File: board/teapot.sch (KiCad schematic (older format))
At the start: 13 parts

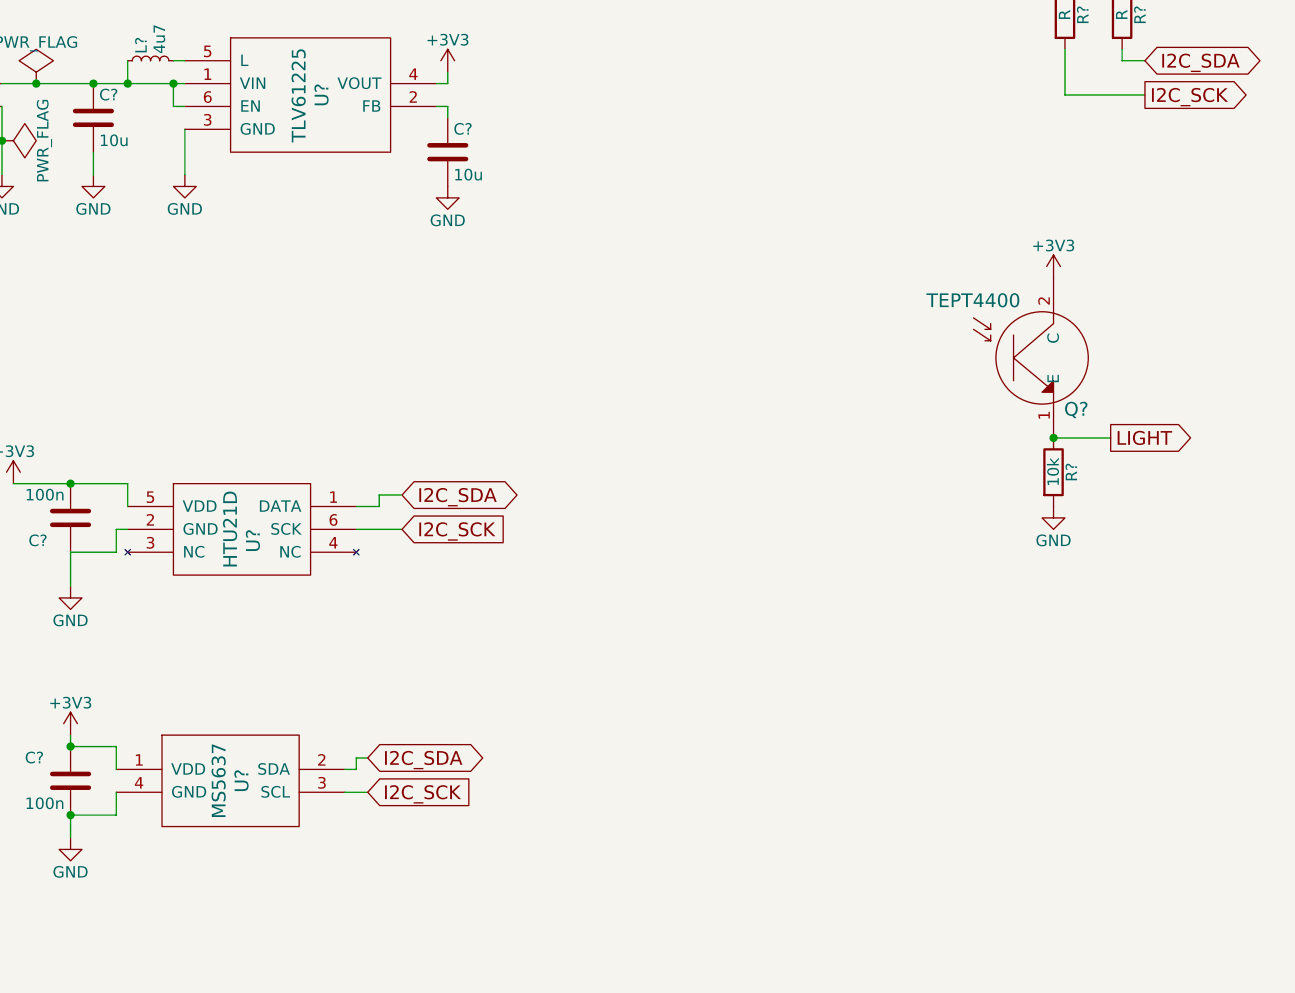
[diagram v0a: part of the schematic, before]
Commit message: schematic part for STM32F070F6P6
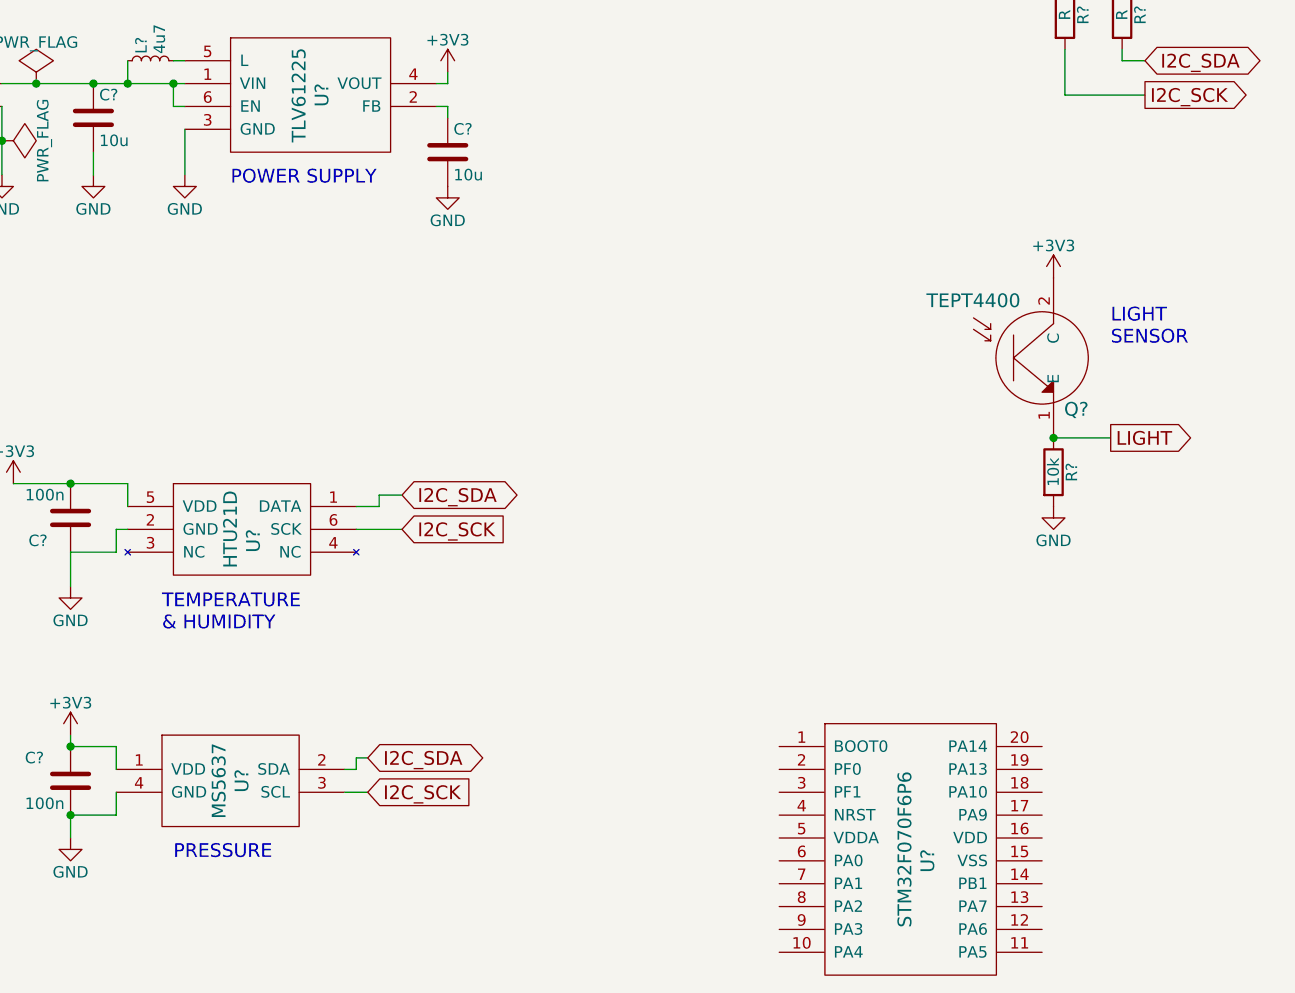
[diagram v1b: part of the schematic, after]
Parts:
- added U?: STM32F070F6P6, symbol STM32F070F6P6
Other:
- note added: "LIGHT\nSENSOR"
- note added: "POWER SUPPLY"
- note added: "PRESSURE"
- note added: "TEMPERATURE\n& HUMIDITY"
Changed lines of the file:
@@
 LIBS:ms5637
 LIBS:tept
+LIBS:stm32f070f6p6
 LIBS:teapot-cache
 EELAYER 25 0
@@
 Text GLabel 5850 2900 2    60   Output ~ 0
 LIGHT
+Text Notes 1750 4750 0    60   ~ 0
+PRESSURE
+Text Notes 1700 3750 0    60   ~ 0
+TEMPERATURE\n& HUMIDITY
+Text Notes 2000 1800 0    60   ~ 0
+POWER SUPPLY
+Text Notes 5850 2500 0    60   ~ 0
+LIGHT\nSENSOR
+$Comp
+L STM32F070F6P6 U?
+U 1 1 5670B075
+P 4950 4750
+F 0 "U?" V 5050 4750 60  0000 C CNN
+F 1 "STM32F070F6P6" V 4950 4800 60  0000 C CNN
+F 2 "" H 5250 5450 60  0000 C CNN
+F 3 "" H 5250 5450 60  0000 C CNN
+	1    4950 4750
+	1    0    0    -1
+$EndComp
 $EndSCHEMATC

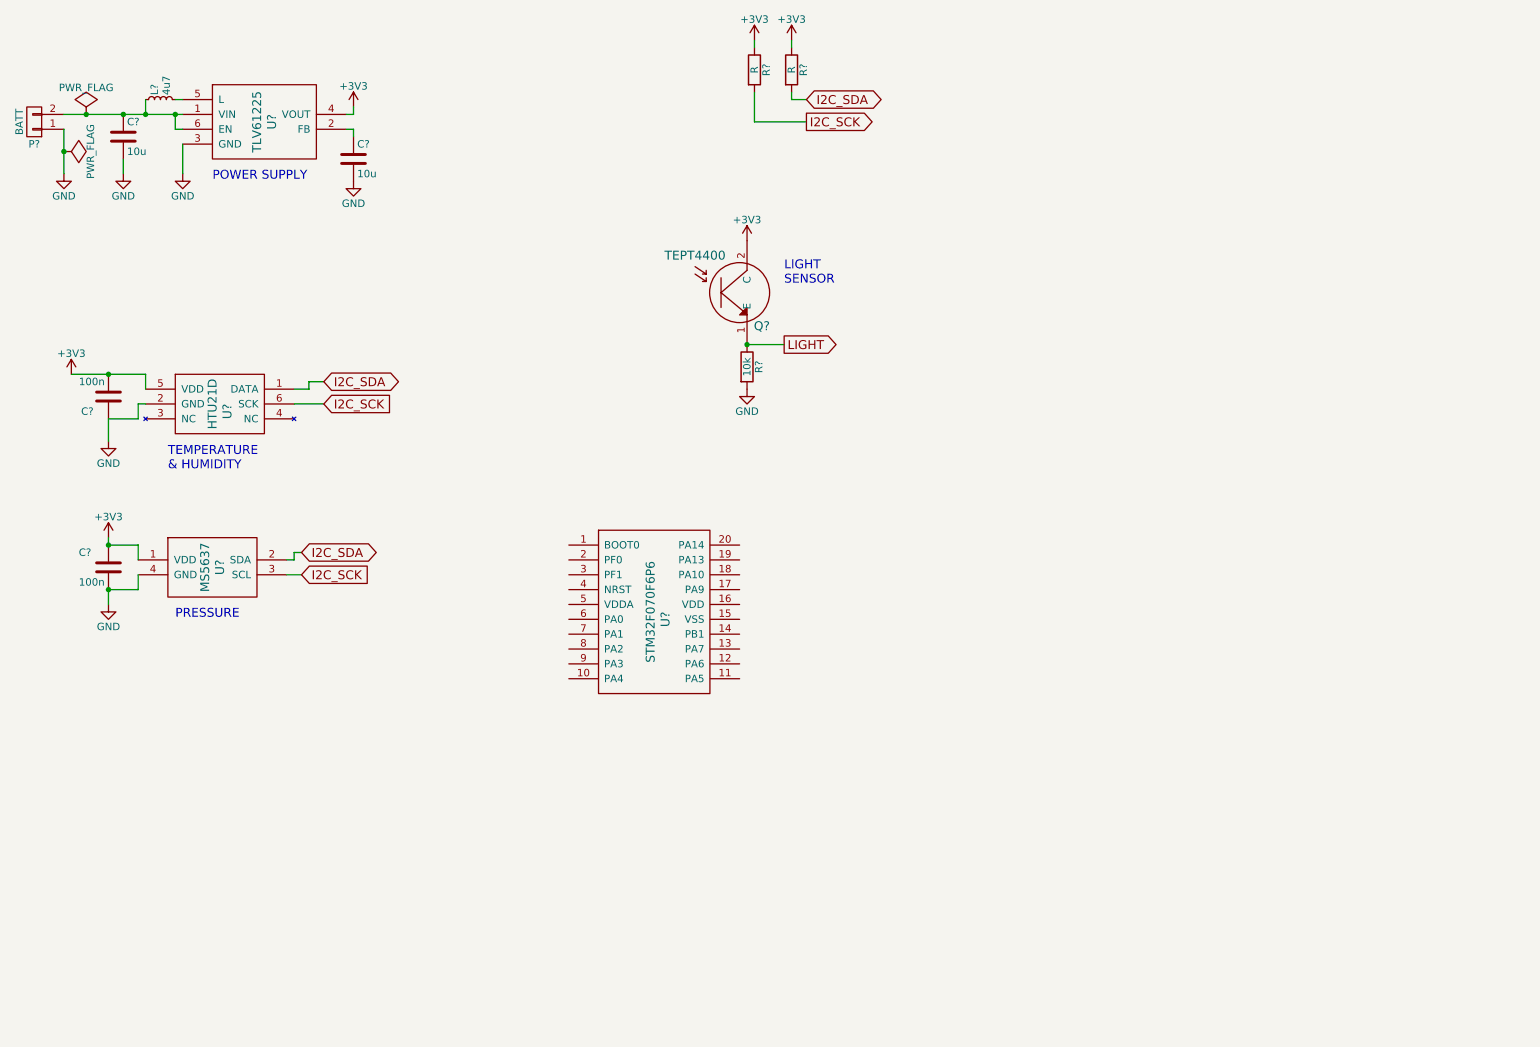
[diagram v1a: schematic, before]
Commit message: Added RFM95W, uC support stuff
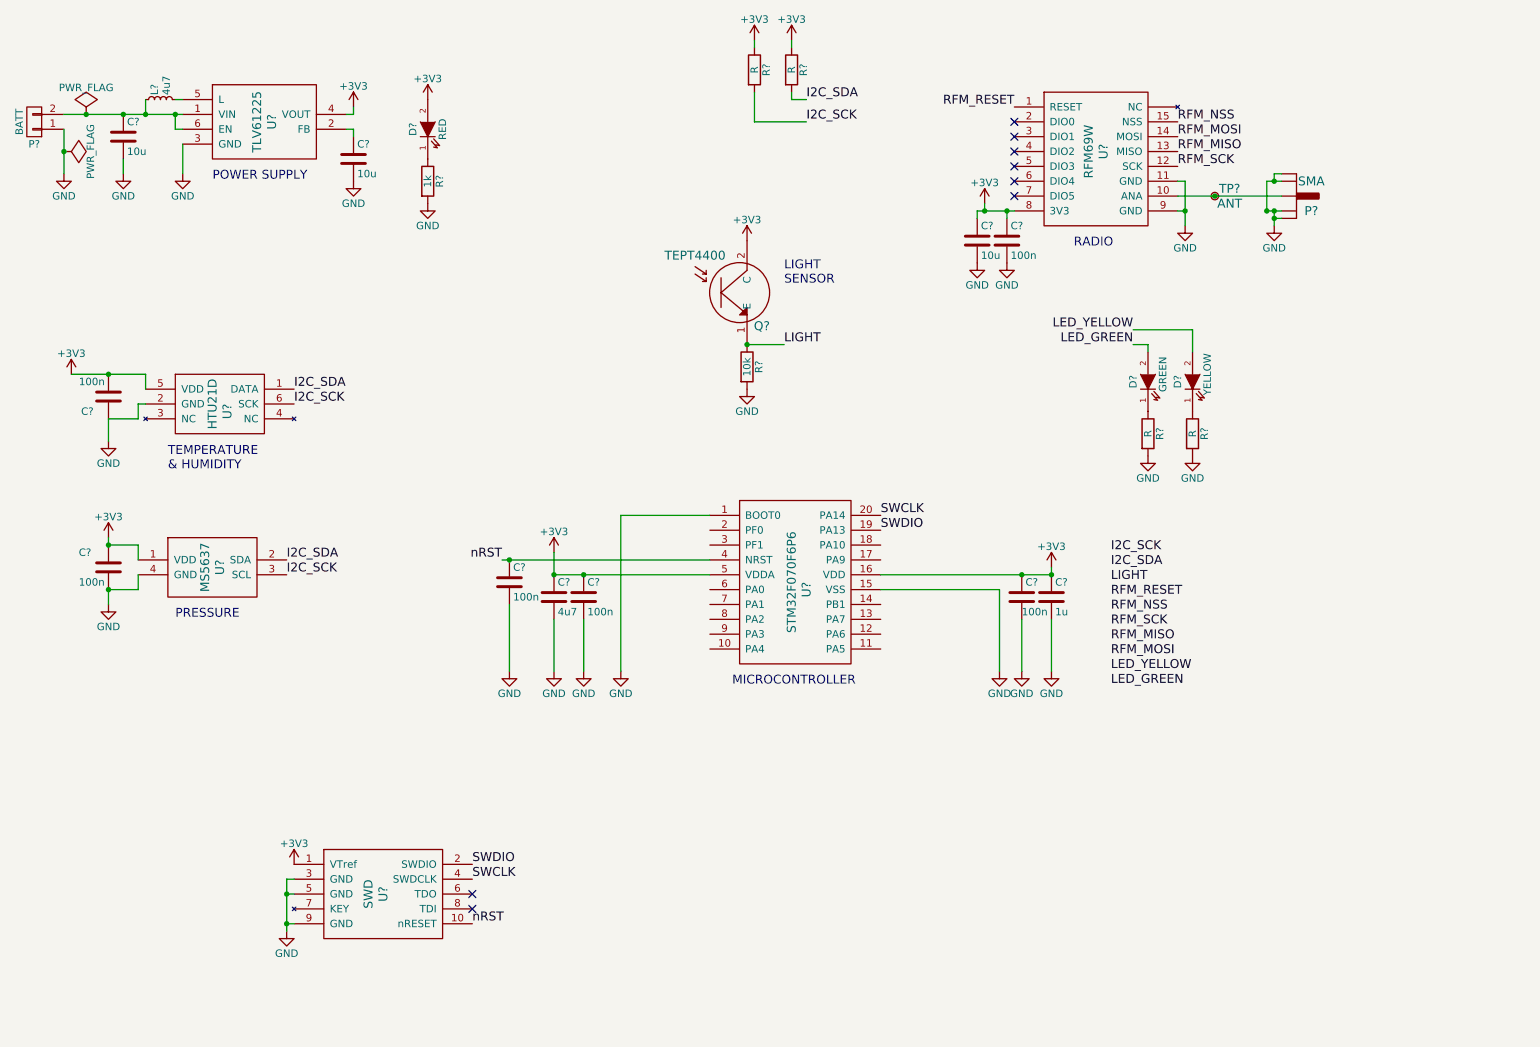
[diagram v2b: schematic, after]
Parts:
- added C? (x4): 100n, symbol C
- added C?: 10u, symbol C
- added C?: 1u, symbol C
- added C?: 4u7, symbol C
- added D?: RED, symbol LED
- added D?: GREEN, symbol LED
- added D?: YELLOW, symbol LED
- added P?: SMA, symbol SMA
- added R?: 1k, symbol R
- added R? (x2): R, symbol R
- added TP?: ANT, symbol TestPoint
- added U?: RFM69W, symbol RFM69W
- added U?: SWD, symbol SWD
- U?: Farnell (none) -> 2488284
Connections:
- net +3V3: now also U?.16 (VDD), U?.5 (VDDA), C?.1, C?.1, C?.1, C?.1, C?.1, C?.1, D?.2 (A), U?.1 (VTref), U?.8 (3V3)
- net GND: now also U?.1 (BOOT0), U?.15 (VSS), C?.2, C?.2, C?.2, C?.2, C?.2, C?.2, C?.2, P?.2 (GND), P?.3 (GND), P?.4 (GND), P?.5 (GND), R?.2, R?.2, R?.2, U?.11 (GND), U?.3 (GND), U?.5 (GND), U?.9 (GND), U?.9 (GND)
- net SWDIO: now reaches U?.19 (PA13)
- net SWDIO: now also U?.2 (SWDIO)
- net SWCLK: now reaches U?.20 (PA14)
- net SWCLK: now also U?.4 (SWDCLK)
- net nRST: now reaches U?.4 (NRST)
- net nRST: now also C?.1, U?.10 (nRESET)
- new net: P?.1 (RF), TP?.1, U?.10 (ANA)
- new net: D?.1 (K), R?.1 (x3)
- new net LED_GREEN: D?.2 (A)
- new net LED_YELLOW: D?.2 (A)
- new net RFM_MISO: U?.13 (MISO)
- new net RFM_MOSI: U?.14 (MOSI)
- new net RFM_NSS: U?.15 (NSS)
- new net RFM_RESET: U?.1 (RESET)
- new net RFM_SCK: U?.12 (SCK)
- no-connect marks 0 -> 8
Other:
- note added: "MICROCONTROLLER"
- note added: "RADIO"
- moved on the sheet: U?

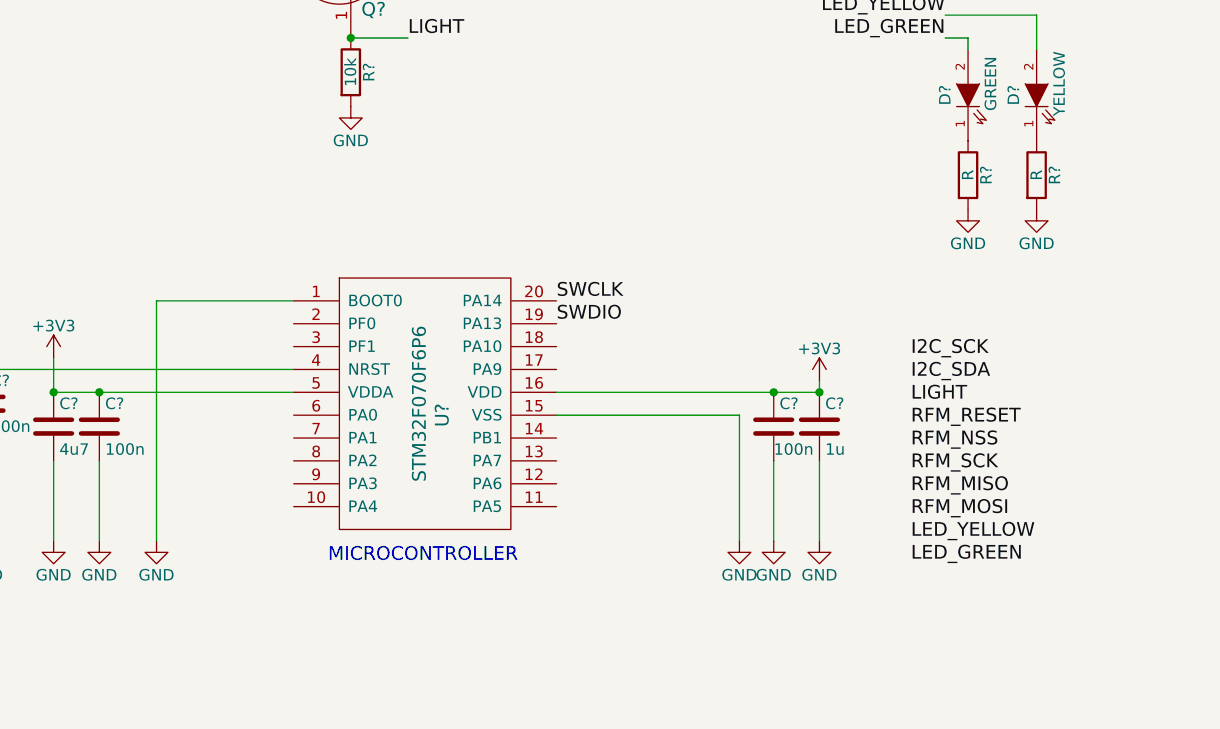
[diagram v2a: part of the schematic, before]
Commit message: Initial uC pin assignment
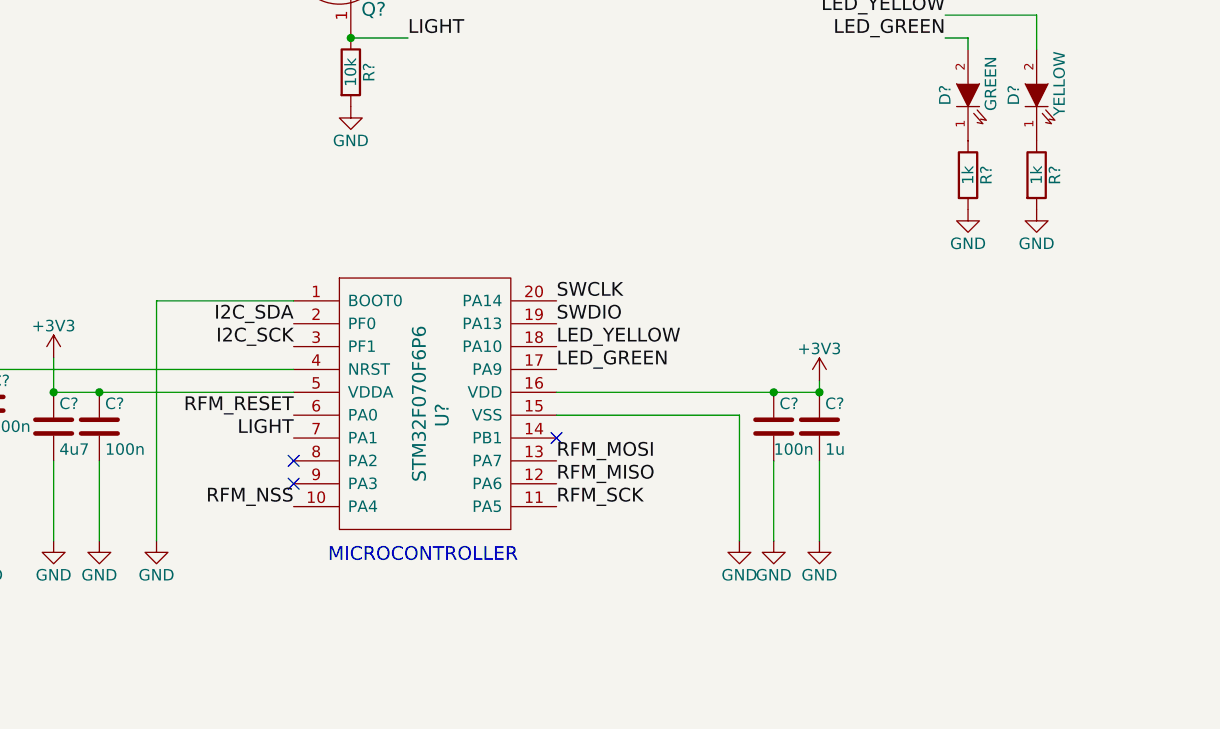
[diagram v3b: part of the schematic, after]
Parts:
- R? (x2): value R -> 1k
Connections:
- net I2C_SCK: now also U?.3 (PF1)
- net I2C_SDA: now also U?.2 (PF0)
- net LED_GREEN: now also U?.17 (PA9)
- net LED_YELLOW: now also U?.18 (PA10)
- net LIGHT: now also U?.7 (PA1)
- net RFM_MISO: now also U?.12 (PA6)
- net RFM_MOSI: now also U?.13 (PA7)
- net RFM_NSS: now also U?.10 (PA4)
- net RFM_RESET: now also U?.6 (PA0)
- net RFM_SCK: now also U?.11 (PA5)
- no-connect marks 8 -> 11
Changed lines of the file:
@@
 Text Notes 7800 2250 0    60   ~ 0
 RADIO
-Text Label 8050 4300 0    60   ~ 0
+Text Label 5350 4250 2    60   ~ 0
 I2C_SCK
-Text Label 8050 4400 0    60   ~ 0
+Text Label 5350 4150 2    60   ~ 0
 I2C_SDA
-Text Label 8050 4500 0    60   ~ 0
+Text Label 5350 4650 2    60   ~ 0
 LIGHT
-Text Label 8050 4600 0    60   ~ 0
+Text Label 5350 4550 2    60   ~ 0
 RFM_RESET
-Text Label 8050 4700 0    60   ~ 0
+Text Label 5350 4950 2    60   ~ 0
 RFM_NSS
-Text Label 8050 4800 0    60   ~ 0
+Text Label 6500 4950 0    60   ~ 0
 RFM_SCK
-Text Label 8050 4900 0    60   ~ 0
+Text Label 6500 4850 0    60   ~ 0
 RFM_MISO
-Text Label 8050 5000 0    60   ~ 0
+Text Label 6500 4750 0    60   ~ 0
 RFM_MOSI
 $Comp
@@
 	1    0    0    -1
 $EndComp
-Text Label 8050 5100 0    60   ~ 0
+Text Label 6500 4250 0    60   ~ 0
 LED_YELLOW
-Text Label 8050 5200 0    60   ~ 0
+Text Label 6500 4350 0    60   ~ 0
 LED_GREEN
 Text Label 8200 2800 2    60   ~ 0
@@
 P 8300 3500
 F 0 "R?" V 8380 3500 50  0000 C CNN
-F 1 "R" V 8300 3500 50  0000 C CNN
+F 1 "1k" V 8300 3500 50  0000 C CNN
 F 2 "" V 8230 3500 50  0000 C CNN
 F 3 "" H 8300 3500 50  0000 C CNN
@@
 P 8600 3500
 F 0 "R?" V 8680 3500 50  0000 C CNN
-F 1 "R" V 8600 3500 50  0000 C CNN
+F 1 "1k" V 8600 3500 50  0000 C CNN
 F 2 "" V 8530 3500 50  0000 C CNN
 F 3 "" H 8600 3500 50  0000 C CNN
@@
 Text Notes 5500 5200 0    60   ~ 0
 MICROCONTROLLER
+NoConn ~ 6500 4650
+NoConn ~ 5350 4750
+NoConn ~ 5350 4850
 $EndSCHEMATC
